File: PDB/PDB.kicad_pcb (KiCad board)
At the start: 2 copper layers, 7 parts

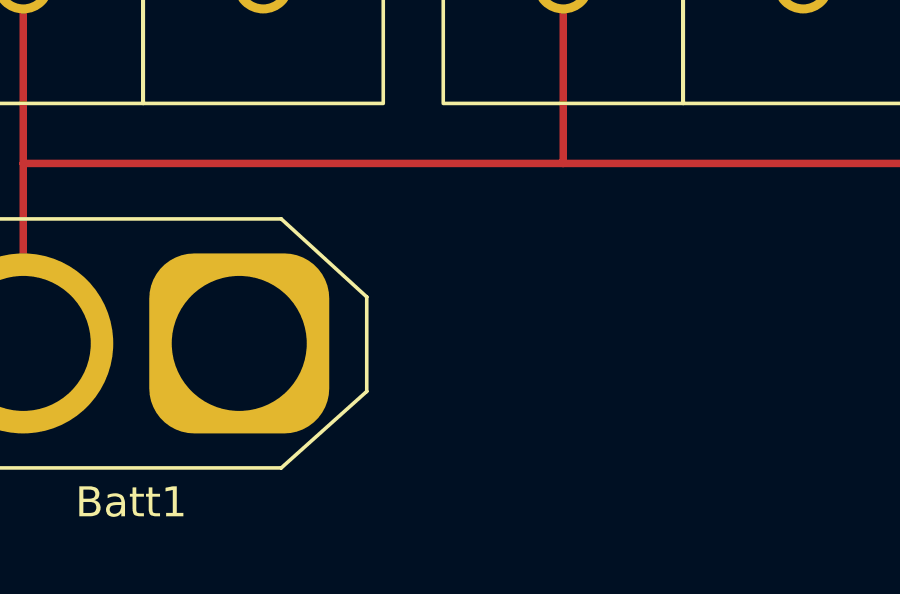
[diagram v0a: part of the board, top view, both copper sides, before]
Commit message: added footprint to de cap
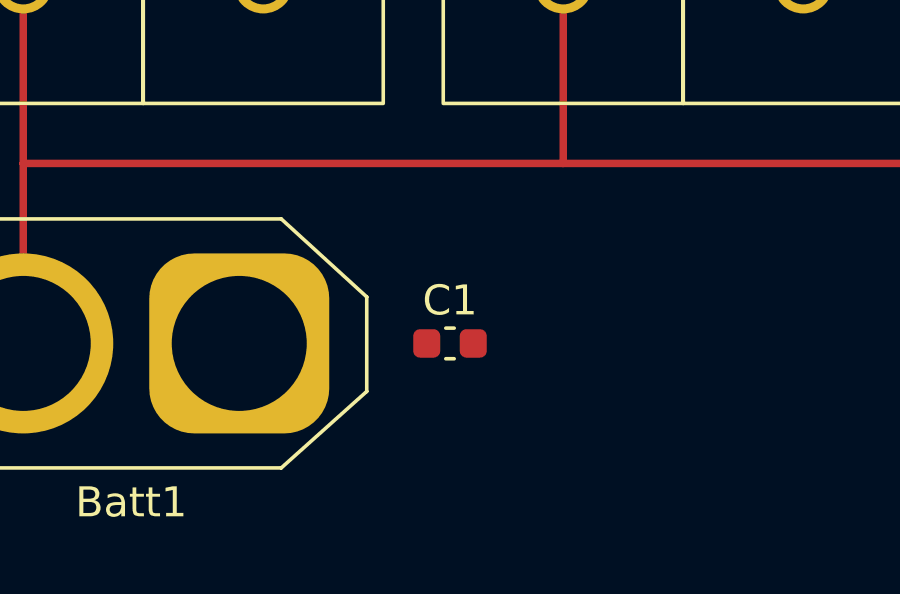
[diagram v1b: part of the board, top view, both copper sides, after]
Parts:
- added C1: C, Capacitor_SMD:C_0603_1608Metric, F.Cu at (33.2, 31.0)
- Batt1: value XT60_F -> Battery
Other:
- board text added: "Power Distribution Board Pioneers in Engineering 2022 something something idk"

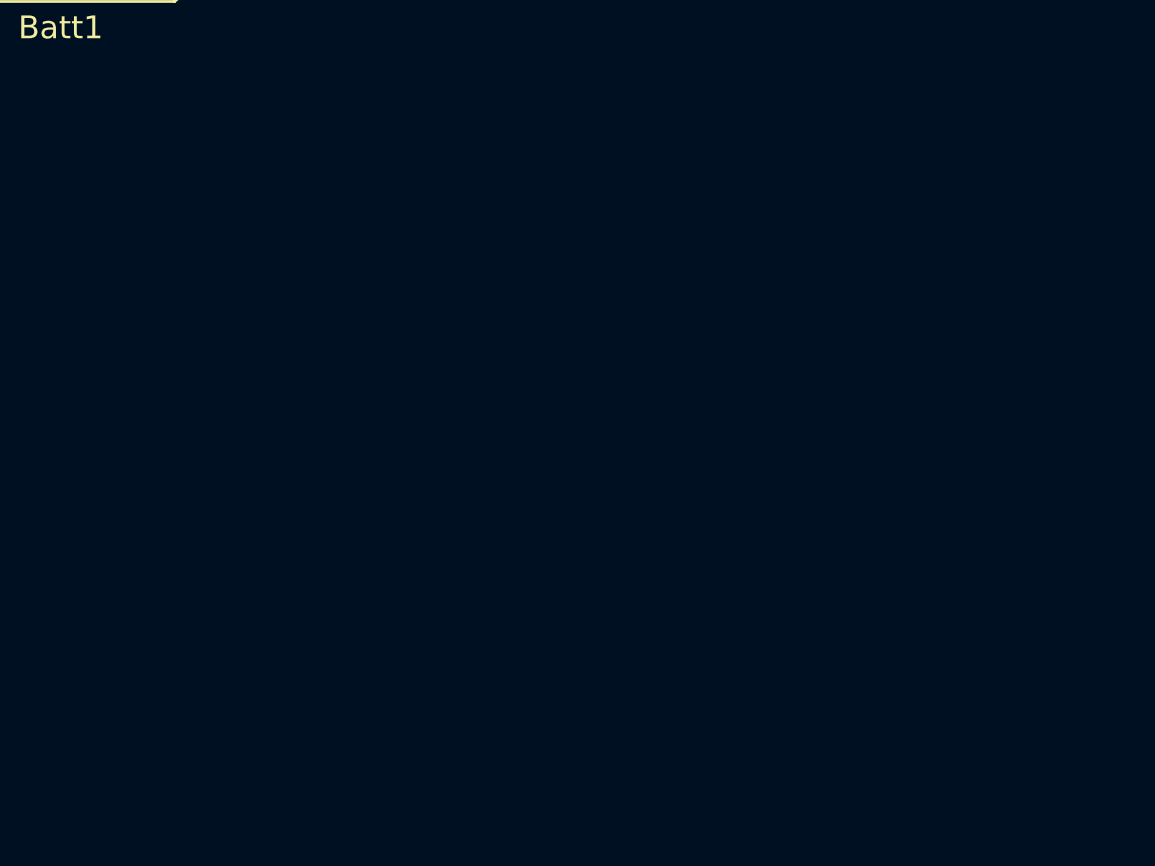
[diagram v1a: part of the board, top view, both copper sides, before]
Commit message: added 5v rail and molex connectors
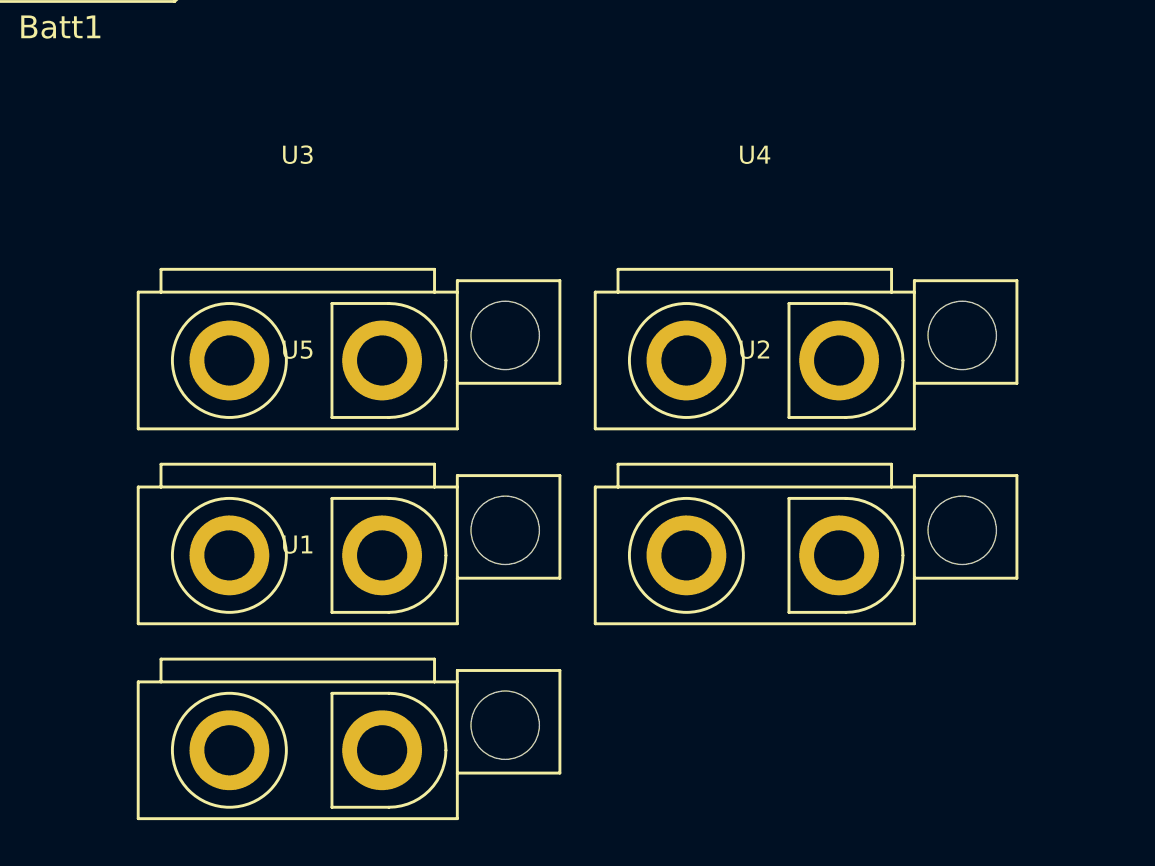
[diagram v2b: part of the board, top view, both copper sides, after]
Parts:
- added U1: 2_pin_molex, PiE_Footprints:ATX, F.Cu at (33.0, 68.0)
- added U2: 2_pin_molex, PiE_Footprints:ATX, F.Cu at (53.0, 59.5)
- added U3: 2_pin_molex, PiE_Footprints:ATX, F.Cu at (33.0, 50.9)
- added U4: 2_pin_molex, PiE_Footprints:ATX, F.Cu at (53.0, 50.9)
- added U5: 2_pin_molex, PiE_Footprints:ATX, F.Cu at (33.0, 59.5)
- Batt1: value Battery -> XT60_F

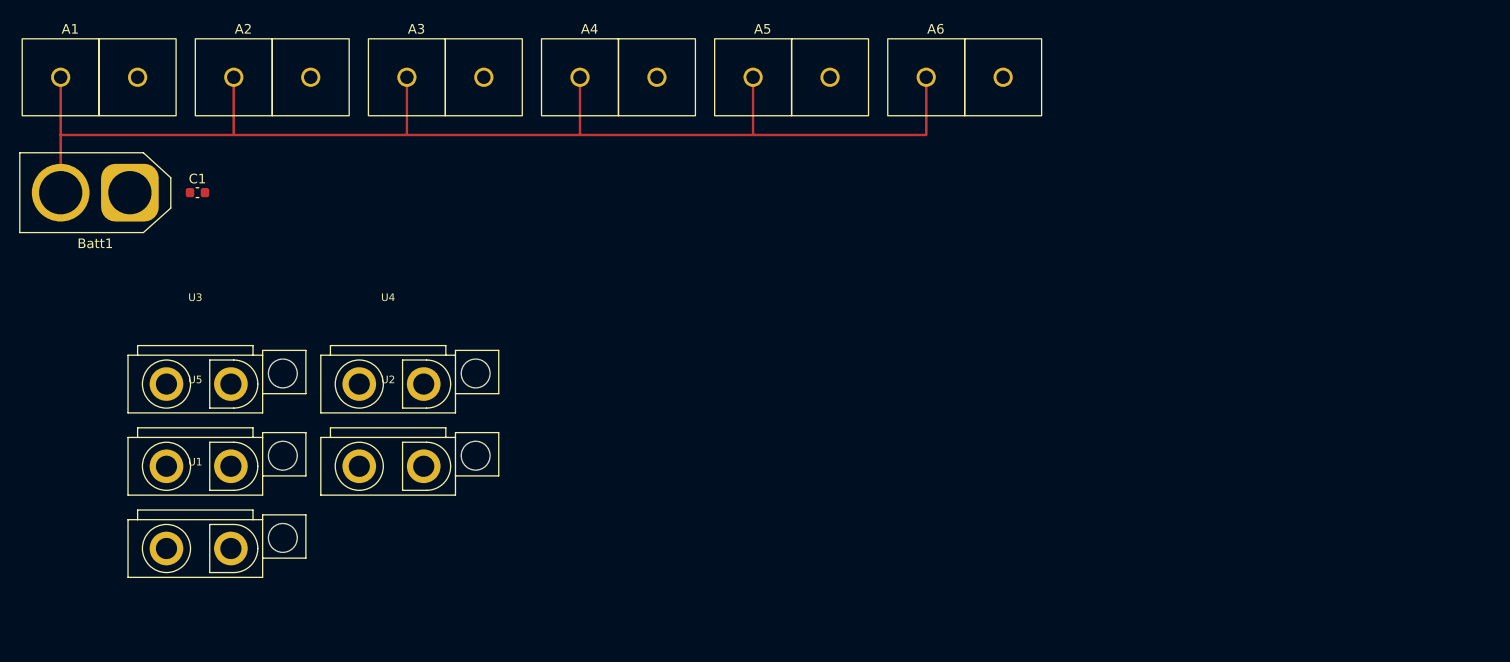
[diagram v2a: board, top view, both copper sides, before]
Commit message: added Converter symbol/footprint
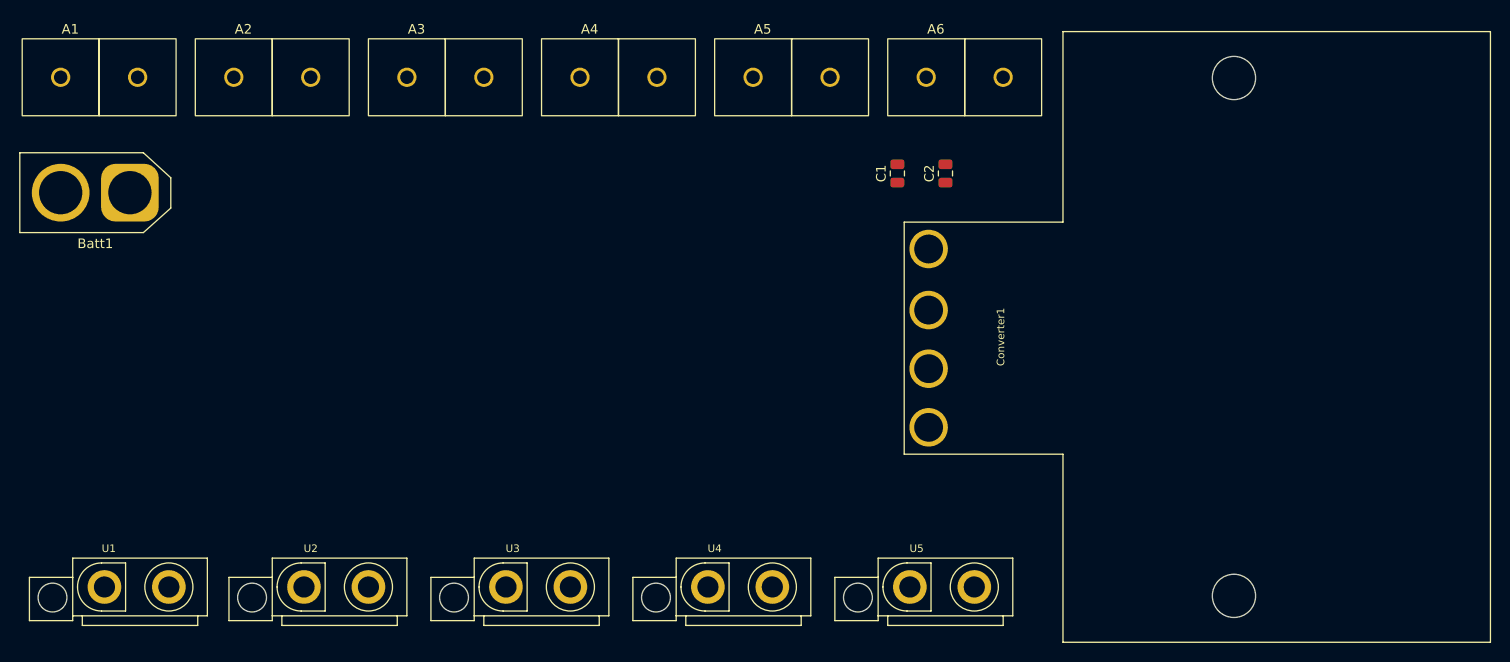
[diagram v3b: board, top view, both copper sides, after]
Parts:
- added C2: 10u, Capacitor_SMD:C_0805_2012Metric, F.Cu at (111.0, 29.0)
- added Converter1: 5v_converter, PiE_Footprints:5v_converter, F.Cu at (141.0, 46.0)
- C1: value C -> 10u; footprint Capacitor_SMD:C_0603_1608Metric -> Capacitor_SMD:C_0805_2012Metric
- U1, U2, U3, U4, U5: footprint PiE_Footprints:ATX -> PiE_Footprints:2_pin_molex
- moved U5 79.0 mm to (111.0, 72.0), turned to 180 degrees
- moved C1 72.8 mm to (106.0, 29.0), turned to 90 degrees
- moved U4 42.6 mm to (90.0, 72.0), turned to 180 degrees
- moved U3 41.7 mm to (69.0, 72.0), turned to 180 degrees
- moved U2 13.5 mm to (48.0, 72.0), turned to 180 degrees
- moved U1 7.00 mm to (27.2, 72.0), turned to 180 degrees
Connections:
- U1 pad 2: unconnected-(U1-Pad2) -> GND
- U2 pad 2: unconnected-(U2-Pad2) -> GND
- U3 pad 2: unconnected-(U3-Pad2) -> GND
- U4 pad 2: unconnected-(U4-Pad2) -> GND
- U5 pad 2: unconnected-(U5-Pad2) -> GND
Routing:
- net /12v: track 132.0 -> 0.00 mm

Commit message: Started footprints
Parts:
- removed U1, U2, U3, U4, U5: 2_pin_molex, PiE_Footprints:2_pin_molex
- added B1: Buzzer, PiE_Footprints:Buzzer, F.Cu at (173.1, 35.3)
- added D1: LED, LED_SMD:LED_0201_0603Metric, F.Cu at (119.1, 56.8)
- added D2: LED, LED_SMD:LED_0201_0603Metric, F.Cu at (119.1, 55.0)
- added D3: 4_digit_7_segment_display, PiE_Footprints:LED-SEG-TH_12P-L30.0-W13.7-P2.54-S10.16-BL, F.Cu at (34.8, 26.7)
- added F1: Fuseholder, PiE_Footprints:Fuse Holder SMD, F.Cu at (111.3, 33.0)
- added JP1: Jumper_2_Open, Connector_PinHeader_2.54mm:PinHeader_1x02_P2.54mm_Vertical, F.Cu at (120.0, 71.3)
- added Jst1: JST-XH_4-pin, PiE_Footprints:JST_XH_B4B-XH-AM_1x04_P2.50mm_Vertical, F.Cu at (90.7, 103.2)
- added Pro1: ProMicro, PiE_Footprints:ProMicro-EnforcedTop, F.Cu at (39.0, 70.0)
- added Q1: S8050, Package_TO_SOT_THT:TO-92_Inline, F.Cu at (133.4, 41.0)
- added R1: 30000, Resistor_SMD:R_0603_1608Metric, F.Cu at (119.0, 85.0)
- added R10: 200, Resistor_SMD:R_0603_1608Metric, F.Cu at (33.0, 37.5)
- added R11: 200, Resistor_SMD:R_0603_1608Metric, F.Cu at (36.8, 37.5)
- added R12: 200, Resistor_SMD:R_0603_1608Metric, F.Cu at (40.6, 37.5)
- added R13: 200, Resistor_SMD:R_0603_1608Metric, F.Cu at (44.5, 37.5)
- added R14: 200, Resistor_SMD:R_0603_1608Metric, F.Cu at (48.3, 37.5)
- added R15: 3300, Resistor_SMD:R_0603_1608Metric, F.Cu at (123.0, 77.5)
- added R16: 1000, Resistor_SMD:R_0603_1608Metric, F.Cu at (140.4, 59.8)
- added R17: 590, Resistor_SMD:R_1210_3225Metric, F.Cu at (140.7, 39.8)
- added R18: 120, Resistor_SMD:R_0603_1608Metric, F.Cu at (145.5, 42.0)
- added R2: 10000, Resistor_SMD:R_0603_1608Metric, F.Cu at (124.3, 73.3)
- added R3: 30000, Resistor_SMD:R_0603_1608Metric, F.Cu at (106.8, 100.9)
- added R4: 10000, Resistor_SMD:R_0603_1608Metric, F.Cu at (131.0, 79.0)
- added R5: 30000, Resistor_SMD:R_0603_1608Metric, F.Cu at (93.2, 108.8)
- added R6: 10000, Resistor_SMD:R_0603_1608Metric, F.Cu at (123.0, 80.0)
- added R7: 200, Resistor_SMD:R_0603_1608Metric, F.Cu at (21.6, 37.5)
- added R8: 200, Resistor_SMD:R_0603_1608Metric, F.Cu at (25.4, 37.5)
- added R9: 200, Resistor_SMD:R_0603_1608Metric, F.Cu at (29.2, 37.5)
- added Sw1: D-SWITCH_MR5-111-C5N-BB, PiE_Footprints:Rocker Switch, F.Cu at (108.9, 94.1)
- added USB1: USB, PiE_Footprints:USB-A_female, F.Cu at (157.4, 31.4)
- added USB2: USB, PiE_Footprints:USB-A_female, F.Cu at (147.5, 46.6)
- added USB3: USB, PiE_Footprints:USB-A_female, F.Cu at (129.9, 57.1)
- added USB4: USB, PiE_Footprints:USB-A_female, F.Cu at (108.6, 76.5)
- moved A1 105.4 mm to (96.0, 91.0)
- moved Batt1 102.0 mm to (126.7, 48.7), turned to 0 degrees
- moved A2 100.1 mm to (140.2, 28.9)
- moved Converter1 98.1 mm to (239.0, 50.0)
- moved A4 85.6 mm to (78.5, 100.5)
- moved A6 83.5 mm to (78.5, 91.0)
- moved A3 63.9 mm to (108.9, 54.9)
- moved A5 51.4 mm to (108.9, 64.5)
- moved C2 43.7 mm to (124.5, 70.5), turned to 0 degrees
- moved C1 41.0 mm to (145.7, 39.2), turned to 0 degrees
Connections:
- Batt1 pad 2: /12v -> /switch in
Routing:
- net Net-(D3-Pad11): track 0.00 -> 26.6 mm
- net Net-(D3-Pad10): track 0.00 -> 24.3 mm
- net Net-(D3-Pad7): track 0.00 -> 19.2 mm
- net Net-(D3-Pad1): track 0.00 -> 11.7 mm
- net Net-(D3-Pad2): track 0.00 -> 10.5 mm
- net Net-(D3-Pad3): track 0.00 -> 6.68 mm
- net Net-(D3-Pad4): track 0.00 -> 6.15 mm
- net Net-(D3-Pad5): track 0.00 -> 5.63 mm
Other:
- board text removed: "Power Distribution Board Pioneers in Engineering 2022 something something idk"

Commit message: Put most components on board
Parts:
- D1, D2: footprint LED_SMD:LED_0201_0603Metric -> LED_SMD:LED_0603_1608Metric
- Q1: footprint Package_TO_SOT_THT:TO-92_Inline -> PiE_Footprints:s8050 SMD
- moved JP1 101.5 mm to (21.2, 48.1)
- moved R4 101.0 mm to (33.5, 52.7), turned to -90 degrees
- moved R2 99.3 mm to (27.2, 52.7), turned to -90 degrees
- moved R1 99.2 mm to (27.2, 47.6), turned to -90 degrees
- moved Jst1 91.1 mm to (28.6, 36.6), turned to 90 degrees
- moved R3 90.6 mm to (33.5, 47.6), turned to -90 degrees
- moved A2 90.2 mm to (78.4, 94.6)
- moved Batt1 89.7 mm to (40.0, 25.7)
- moved R17 88.5 mm to (64.4, 84.7)
- moved Q1 87.7 mm to (46.5, 52.7)
- moved R6 87.5 mm to (39.9, 52.7), turned to -90 degrees
- moved C1 86.6 mm to (72.1, 84.8)
- moved R15 83.1 mm to (47.1, 43.9)
- moved R16 82.1 mm to (59.1, 48.6)
- moved R5 81.2 mm to (39.9, 47.6), turned to -90 degrees
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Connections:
- Batt1 pad 2: /switch in -> /battery
- F1 pad 1: /switch out -> /battery
- F1 pad 2: /switch out -> /battery
- F1 pad 3: /12v -> /fuse out
- F1 pad 4: /12v -> /fuse out
- Sw1 pad 1: /switch in -> /fuse out
- Sw1 pad 2: /switch out -> /12v
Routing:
- net Net-(D3-Pad11): track 26.6 -> 5.63 mm
- net Net-(D3-Pad10): track 24.3 -> 5.10 mm
- net Net-(D3-Pad7): track 19.2 -> 5.10 mm
- net Net-(D3-Pad1): track 11.7 -> 0.00 mm
- net Net-(D3-Pad2): track 10.5 -> 0.00 mm
- net Net-(D3-Pad3): track 6.68 -> 0.00 mm
- net Net-(D3-Pad4): track 6.15 -> 0.00 mm
- net Net-(D3-Pad5): track 5.63 -> 0.00 mm
